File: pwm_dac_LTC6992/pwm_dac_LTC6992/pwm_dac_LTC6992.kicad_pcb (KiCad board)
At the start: 2 copper layers, 14 parts, among them J2 Screw_Terminal_01x02, J3 Conn_01x03_Male, U1 LTC6992-1 (Rev. D)

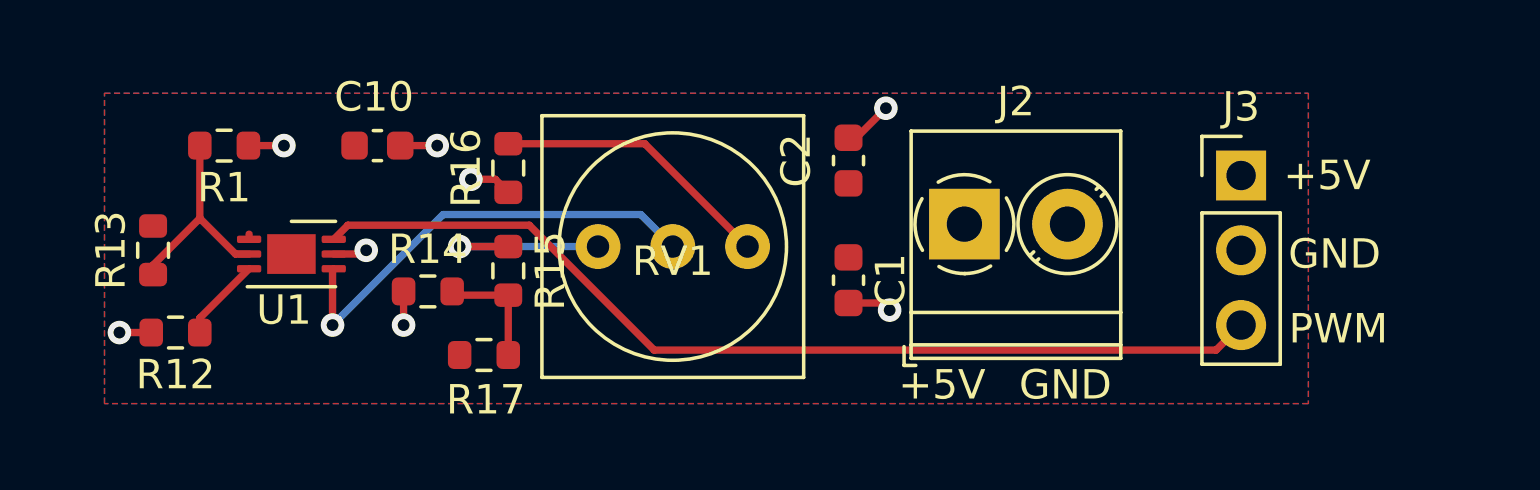
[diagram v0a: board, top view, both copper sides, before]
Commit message: Finished PCB with header output/support
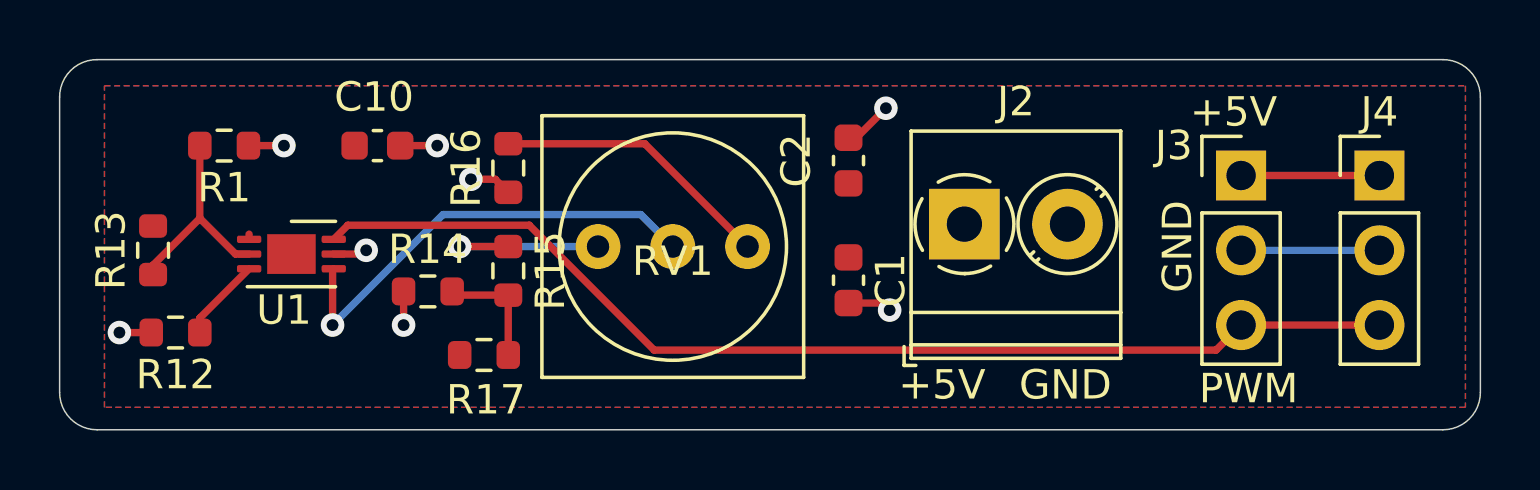
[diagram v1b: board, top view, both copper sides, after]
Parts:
- added J4: Conn_01x03_Male, Connector_PinHeader_2.54mm:PinHeader_1x03_P2.54mm_Vertical, F.Cu at (153.3, 41.7)
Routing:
- net GND: track 10.5 -> 15.2 mm
- net /PWM: track 33.1 -> 37.8 mm
- net +5V: track 0.18 -> 4.87 mm
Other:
- board outline added: 48.3 x 12.6 mm
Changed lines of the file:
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@@
   (general
     (thickness 1.6)
-    (drawings 5)
-    (tracks 50)
+    (drawings 13)
+    (tracks 53)
     (zones 0)
-    (modules 14)
+    (modules 15)
     (nets 10)
   )
@@
     (mod_text_size 1 1)
     (mod_text_width 0.15)
-    (pad_size 1.524 1.524)
-    (pad_drill 0.762)
+    (pad_size 1.7 1.7)
+    (pad_drill 1)
     (pad_to_mask_clearance 0)
     (aux_axis_origin 0 0)
@@
     (add_net "Net-(R15-Pad1)")
     (add_net "Net-(R16-Pad2)")
+  )
+  (module Connector_PinHeader_2.54mm:PinHeader_1x03_P2.54mm_Vertical (layer F.Cu)
+    (at 153.289 41.656)
+    (descr "Through hole straight pin header, 1x03, 2.54mm pitch, single row")
+    (tags "Through hole pin header THT 1x03 2.54mm single row")
+    (fp_text reference J4 (at 0 -2.159) (layer F.SilkS)
+      (effects (font (size 1 1) (thickness 0.15)))
+    )
+    (fp_text value Conn_01x03_Male (at 0 7.41) (layer F.Fab)
+      (effects (font (size 1 1) (thickness 0.15)))
+    )
+    (fp_text user %R (at 0 2.54 90) (layer F.Fab)
+      (effects (font (size 1 1) (thickness 0.15)))
+    )
+    (fp_line (start 1.8 -1.8) (end -1.8 -1.8) (layer F.CrtYd) (width 0.05))
+    (fp_line (start 1.8 6.85) (end 1.8 -1.8) (layer F.CrtYd) (width 0.05))
+    (fp_line (start -1.8 6.85) (end 1.8 6.85) (layer F.CrtYd) (width 0.05))
+    (fp_line (start -1.8 -1.8) (end -1.8 6.85) (layer F.CrtYd) (width 0.05))
+    (fp_line (start -1.33 -1.33) (end 0 -1.33) (layer F.SilkS) (width 0.12))
+    (fp_line (start -1.33 0) (end -1.33 -1.33) (layer F.SilkS) (width 0.12))
+    (fp_line (start -1.33 1.27) (end 1.33 1.27) (layer F.SilkS) (width 0.12))
+    (fp_line (start 1.33 1.27) (end 1.33 6.41) (layer F.SilkS) (width 0.12))
+    (fp_line (start -1.33 1.27) (end -1.33 6.41) (layer F.SilkS) (width 0.12))
+    (fp_line (start -1.33 6.41) (end 1.33 6.41) (layer F.SilkS) (width 0.12))
+    (fp_line (start -1.27 -0.635) (end -0.635 -1.27) (layer F.Fab) (width 0.1))
+    (fp_line (start -1.27 6.35) (end -1.27 -0.635) (layer F.Fab) (width 0.1))
+    (fp_line (start 1.27 6.35) (end -1.27 6.35) (layer F.Fab) (width 0.1))
+    (fp_line (start 1.27 -1.27) (end 1.27 6.35) (layer F.Fab) (width 0.1))
+    (fp_line (start -0.635 -1.27) (end 1.27 -1.27) (layer F.Fab) (width 0.1))
+    (pad 3 thru_hole oval (at 0 5.08) (size 1.7 1.7) (drill 1) (layers *.Cu *.Mask)
+      (net 3 /PWM))
+    (pad 2 thru_hole oval (at 0 2.54) (size 1.7 1.7) (drill 1) (layers *.Cu *.Mask)
+      (net 1 GND))
+    (pad 1 thru_hole rect (at 0 0) (size 1.7 1.7) (drill 1) (layers *.Cu *.Mask)
+      (net 2 +5V))
+    (model ${KISYS3DMOD}/Connector_PinHeader_2.54mm.3dshapes/PinHeader_1x03_P2.54mm_Vertical.wrl
+      (at (xyz 0 0 0))
+      (scale (xyz 1 1 1))
+      (rotate (xyz 0 0 0))
+    )
   )
   (module Capacitor_SMD:C_0603_1608Metric (layer F.Cu)
@@
     (descr "Through hole straight pin header, 1x03, 2.54mm pitch, single row")
     (tags "Through hole pin header THT 1x03 2.54mm single row")
-    (fp_text reference J3 (at 0 -2.33) (layer F.SilkS)
+    (fp_text reference J3 (at -2.286 -1.016) (layer F.SilkS)
       (effects (font (size 1 1) (thickness 0.15)))
     )
@@
     )
   )
-  (gr_text PWM (at 151.892 46.863) (layer F.SilkS)
+  (gr_line (start 156.718 38.989) (end 156.718 49.022) (layer Edge.Cuts) (width 0.05))
+  (gr_line (start 108.458 38.989) (end 108.458 49.022) (layer Edge.Cuts) (width 0.05))
+  (gr_line (start 109.728 37.719) (end 155.448 37.719) (layer Edge.Cuts) (width 0.05))
+  (gr_line (start 155.448 50.292) (end 109.728 50.292) (layer Edge.Cuts) (width 0.05))
+  (gr_arc (start 109.728 38.989) (end 109.728 37.719) (angle -90) (layer Edge.Cuts) (width 0.05))
+  (gr_arc (start 109.728 49.022) (end 108.458 49.022) (angle -90) (layer Edge.Cuts) (width 0.05))
+  (gr_arc (start 155.448 49.022) (end 155.448 50.292) (angle -90) (layer Edge.Cuts) (width 0.05))
+  (gr_arc (start 155.448 38.989) (end 156.718 38.989) (angle -90) (layer Edge.Cuts) (width 0.05))
+  (gr_text PWM (at 148.844 48.895) (layer F.SilkS)
     (effects (font (size 1 1) (thickness 0.15)))
   )
-  (gr_text GND (at 151.765 44.323) (layer F.SilkS)
+  (gr_text GND (at 146.431 44.069 90) (layer F.SilkS)
     (effects (font (size 1 1) (thickness 0.15)))
   )
@@
     (effects (font (size 1 1) (thickness 0.15)))
   )
-  (gr_text +5V (at 151.511 41.656) (layer F.SilkS)
+  (gr_text +5V (at 148.336 39.497) (layer F.SilkS)
     (effects (font (size 1 1) (thickness 0.15)))
   )
@@
   (segment (start 136.411 45.987) (end 136.652 46.228) (width 0.25) (layer F.Cu) (net 1))
   (segment (start 135.255 45.987) (end 136.411 45.987) (width 0.25) (layer F.Cu) (net 1))
+  (segment (start 148.59 44.196) (end 153.289 44.196) (width 0.25) (layer B.Cu) (net 1))
   (segment (start 114.8945 43.823) (end 114.8945 43.6475) (width 0.25) (layer F.Cu) (net 2))
+  (segment (start 148.59 41.656) (end 153.289 41.656) (width 0.25) (layer F.Cu) (net 2))
   (segment (start 147.740001 47.585999) (end 148.59 46.736) (width 0.25) (layer F.Cu) (net 3))
   (segment (start 128.654237 47.585999) (end 147.740001 47.585999) (width 0.25) (layer F.Cu) (net 3))
@@
   (segment (start 118.24851 43.34399) (end 124.412228 43.34399) (width 0.25) (layer F.Cu) (net 3))
   (segment (start 117.7695 43.823) (end 118.24851 43.34399) (width 0.25) (layer F.Cu) (net 3))
+  (segment (start 148.59 46.736) (end 153.289 46.736) (width 0.25) (layer F.Cu) (net 3))
   (segment (start 114.433978 44.323) (end 114.8945 44.323) (width 0.25) (layer F.Cu) (net 4))
   (segment (start 113.221 43.110022) (end 114.433978 44.323) (width 0.25) (layer F.Cu) (net 4))
@@
     (polygon
       (pts
-        (xy 150.876 49.403) (xy 109.982 49.403) (xy 109.982 38.862) (xy 150.876 38.862)
+        (xy 156.21 49.53) (xy 109.982 49.53) (xy 109.982 38.608) (xy 156.21 38.608)
       )
     )
@@
     (polygon
       (pts
-        (xy 150.876 49.403) (xy 109.982 49.403) (xy 109.982 38.862) (xy 150.876 38.862)
+        (xy 156.21 49.53) (xy 109.982 49.53) (xy 109.982 38.608) (xy 156.21 38.608)
       )
     )
